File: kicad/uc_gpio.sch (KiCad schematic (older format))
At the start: 1 part, among them U1_501 TMS320F28388DZWTS

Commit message: passed all footprint, preliminarly.. and taken a pic
I've passed all 3d models, and make a pic of that, it's the first
impresion, but it need's more indeed reviews
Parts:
- renumbered U1_501 to U301
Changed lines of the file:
@@
 LCD_GPIO4
 $Comp
-L servo:TMS320F28388 U1_501
+L servo:TMS320F28388 U301
 U 2 1 5DB38FFC
 P 5900 6300
-F 0 "U1_501" H 5900 10873 60  0000 C CNN
+F 0 "U301" H 5900 10873 60  0000 C CNN
 F 1 "TMS320F28388DZWTS" H 5900 10775 50  0000 C CNN
 F 2 "servo:BGA337CP80_19X19_1600X1600X140B50N" H 5900 6300 50  0001 C CNN

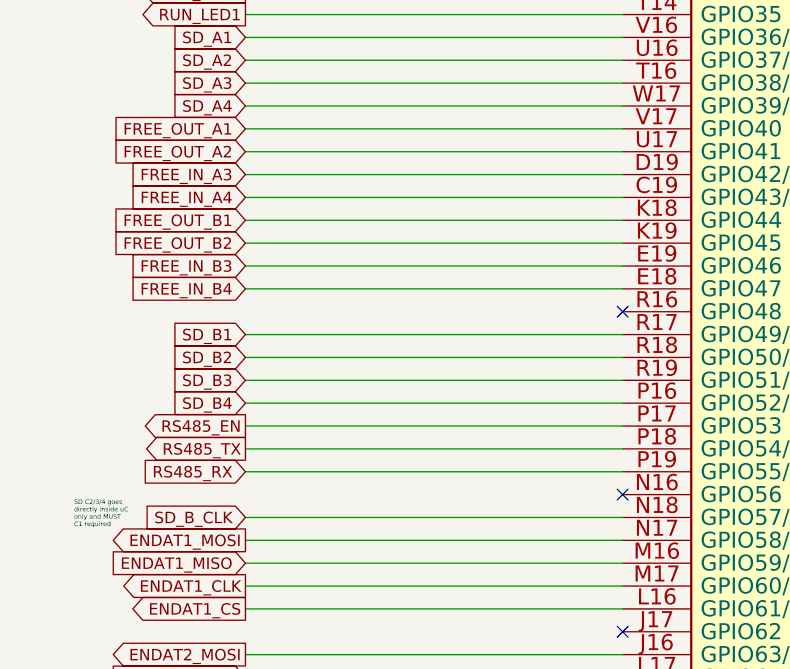
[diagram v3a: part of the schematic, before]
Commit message: I've reducede the PCB size ADC TVS, USB host and IDC out
TVS for ADC protection, USB out 'cause it's almost free and IDC debug
out in an IDC. Better and thinner terminal block connector help in
reduce the board size.
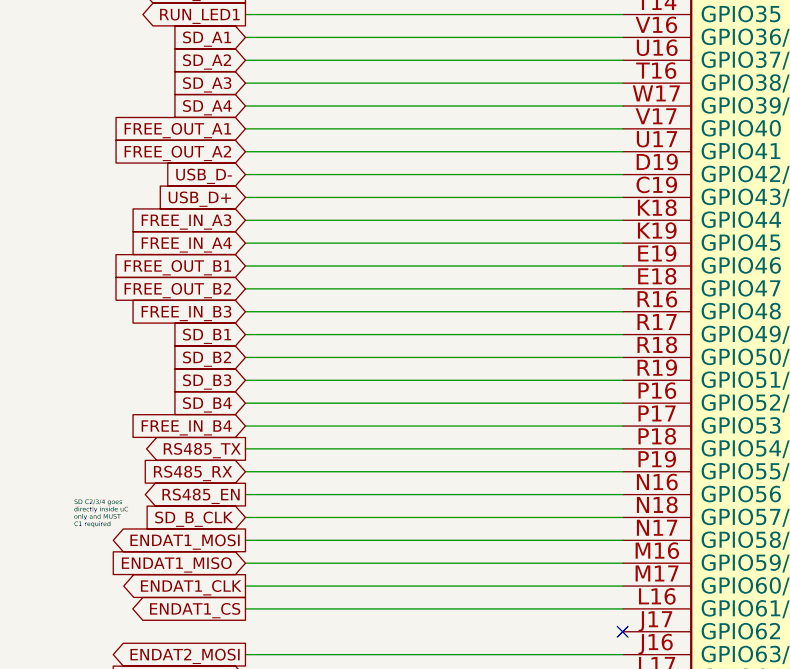
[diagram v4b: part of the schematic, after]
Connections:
- net FREE_IN_A3: now also U301.K18 (GPIO44); no longer U301.D19 (GPIO42/USB0DM)
- net FREE_IN_A4: now also U301.K19 (GPIO45); no longer U301.C19 (GPIO43/USB0DP)
- net FREE_IN_B3: now also U301.R16 (GPIO48); no longer U301.E19 (GPIO46)
- net FREE_IN_B4: now also U301.P17 (GPIO53); no longer U301.E18 (GPIO47)
- net FREE_OUT_B1: now also U301.E19 (GPIO46); no longer U301.K18 (GPIO44)
- net FREE_OUT_B2: now also U301.E18 (GPIO47); no longer U301.K19 (GPIO45)
- net RS485_EN: now also U301.N16 (GPIO56); no longer U301.P17 (GPIO53)
- new net USB_D+: U301.C19 (GPIO43/USB0DP)
- new net USB_D-: U301.D19 (GPIO42/USB0DM)
- no-connect marks 23 -> 21
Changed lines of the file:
@@
 Text GLabel 3150 7500 0    50   Output ~ 0
 RS485_TX
-Text GLabel 3150 7400 0    50   Output ~ 0
+Text GLabel 3150 7700 0    50   Output ~ 0
 RS485_EN
 Wire Wire Line
@@
 Text GLabel 3150 6200 0    50   Input ~ 0
 FREE_OUT_A2
-Text GLabel 3150 6300 0    50   Input ~ 0
+Text GLabel 3150 6500 0    50   Input ~ 0
 FREE_IN_A3
-Text GLabel 3150 6400 0    50   Input ~ 0
+Text GLabel 3150 6600 0    50   Input ~ 0
 FREE_IN_A4
-Text GLabel 3150 6500 0    50   Input ~ 0
+Text GLabel 3150 6700 0    50   Input ~ 0
 FREE_OUT_B1
-Text GLabel 3150 6600 0    50   Input ~ 0
+Text GLabel 3150 6800 0    50   Input ~ 0
 FREE_OUT_B2
-Text GLabel 3150 6700 0    50   Input ~ 0
+Text GLabel 3150 6900 0    50   Input ~ 0
 FREE_IN_B3
-Text GLabel 3150 6800 0    50   Input ~ 0
+Text GLabel 3150 7400 0    50   Input ~ 0
 FREE_IN_B4
 Wire Wire Line
@@
 NoConn ~ 4800 9600
 NoConn ~ 4800 9700
-NoConn ~ 4800 6900
-NoConn ~ 4800 7700
 NoConn ~ 4800 8300
 NoConn ~ 8350 3400
@@
 Text GLabel 9700 3200 2    50   Input ~ 0
 LCD_GPIO4
+Wire Wire Line
+	9700 3200 8350 3200
+Wire Wire Line
+	8350 3300 9700 3300
+Text GLabel 3150 6400 0    50   Input ~ 0
+USB_D+
+Text GLabel 3150 6300 0    50   Input ~ 0
+USB_D-
 $Comp
 L servo:TMS320F28388 U301
@@
 $EndComp
 Wire Wire Line
-	9700 3200 8350 3200
-Wire Wire Line
-	8350 3300 9700 3300
+	4800 6900 3150 6900
+Wire Wire Line
+	4800 7700 3150 7700
 $EndSCHEMATC

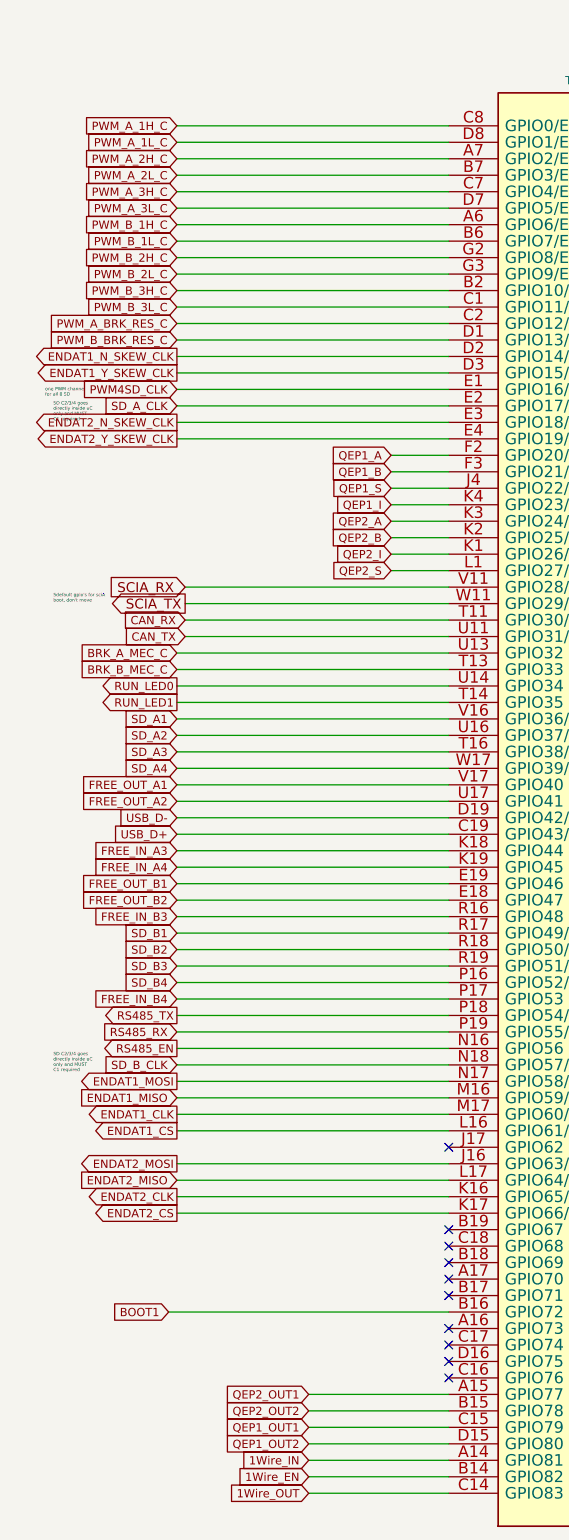
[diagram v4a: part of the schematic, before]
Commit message: I forgot that QUEP was diferential!! all to back....
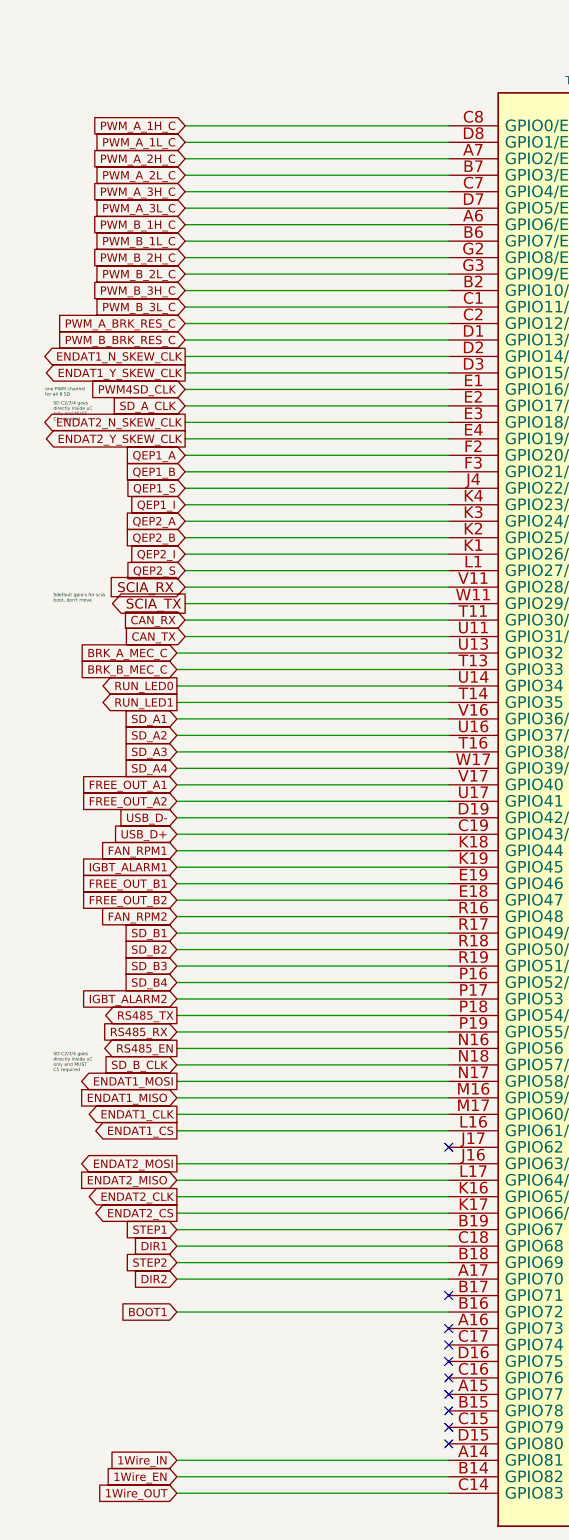
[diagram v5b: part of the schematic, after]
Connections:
- net DIR2: now reaches U301.A17 (GPIO70)
- net STEP2: now reaches U301.B18 (GPIO69)
- net STEP1: now reaches U301.B19 (GPIO67)
- net DIR1: now reaches U301.C18 (GPIO68)
- net FREE_IN_A3 renamed FAN_RPM1
- net FREE_IN_A4 renamed IGBT_ALARM1
- net FREE_IN_B3 renamed FAN_RPM2
- net FREE_IN_B4 renamed IGBT_ALARM2
- net QEP1_OUT1: no longer names the net of U301.C15 (GPIO79)
- net QEP1_OUT2: no longer names the net of U301.D15 (GPIO80)
- net QEP2_OUT1: no longer names the net of U301.A15 (GPIO77)
- net QEP2_OUT2: no longer names the net of U301.B15 (GPIO78)
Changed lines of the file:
@@
 $Descr A3 16535 11693
 encoding utf-8
-Sheet 13 18
+Sheet 13 19
 Title "gpio"
 Date "2020-01-09"
@@
 $EndDescr
 Wire Wire Line
-	3950 10400 4800 10400
-Wire Wire Line
-	3950 10300 4800 10300
-Wire Wire Line
-	3950 10200 4800 10200
-Wire Wire Line
-	3950 10100 4800 10100
-Wire Wire Line
-	3950 10000 4800 10000
-Wire Wire Line
-	3950 9900 4800 9900
-Wire Wire Line
-	3950 9800 4800 9800
-Text GLabel 3150 2100 0    50   Input ~ 0
+	3150 10400 4800 10400
+Wire Wire Line
+	3150 10300 4800 10300
+Wire Wire Line
+	3150 10200 4800 10200
+Text GLabel 3200 2100 0    50   Input ~ 0
 PWM_A_1H_C
-Text GLabel 3150 2300 0    50   Input ~ 0
+Text GLabel 3200 2300 0    50   Input ~ 0
 PWM_A_2H_C
-Text GLabel 3150 2500 0    50   Input ~ 0
+Text GLabel 3200 2500 0    50   Input ~ 0
 PWM_A_3H_C
-Text GLabel 3150 2200 0    50   Input ~ 0
+Text GLabel 3200 2200 0    50   Input ~ 0
 PWM_A_1L_C
-Text GLabel 3150 2400 0    50   Input ~ 0
+Text GLabel 3200 2400 0    50   Input ~ 0
 PWM_A_2L_C
-Text GLabel 3150 2600 0    50   Input ~ 0
+Text GLabel 3200 2600 0    50   Input ~ 0
 PWM_A_3L_C
-Text GLabel 3150 2900 0    50   Input ~ 0
+Text GLabel 3200 2900 0    50   Input ~ 0
 PWM_B_2H_C
-Text GLabel 3150 2700 0    50   Input ~ 0
+Text GLabel 3200 2700 0    50   Input ~ 0
 PWM_B_1H_C
-Text GLabel 3150 2800 0    50   Input ~ 0
+Text GLabel 3200 2800 0    50   Input ~ 0
 PWM_B_1L_C
-Text GLabel 3150 3100 0    50   Input ~ 0
+Text GLabel 3200 3100 0    50   Input ~ 0
 PWM_B_3H_C
-Text GLabel 3150 3200 0    50   Input ~ 0
+Text GLabel 3200 3200 0    50   Input ~ 0
 PWM_B_3L_C
-Text GLabel 3150 3000 0    50   Input ~ 0
+Text GLabel 3200 3000 0    50   Input ~ 0
 PWM_B_2L_C
 Wire Wire Line
@@
 Wire Wire Line
 	3150 5600 4800 5600
-Text GLabel 3100 9300 0    50   Input ~ 0
+Text GLabel 3150 9300 0    50   Input ~ 0
 BOOT1
 Text GLabel 9750 2100 2    50   Input ~ 0
@@
 	8350 2100 9750 2100
 Wire Wire Line
-	3100 9300 4800 9300
+	3150 9300 4800 9300
 Text GLabel 3200 5000 0    60   Output ~ 0
 SCIA_TX
@@
 Wire Wire Line
 	3150 8700 4800 8700
-Text GLabel 4450 4500 0    50   Input ~ 0
+Text GLabel 3200 4500 0    50   Input ~ 0
 QEP2_A
-Text GLabel 4450 4600 0    50   Input ~ 0
+Text GLabel 3200 4600 0    50   Input ~ 0
 QEP2_B
-Text GLabel 4450 4700 0    50   Input ~ 0
+Text GLabel 3200 4700 0    50   Input ~ 0
 QEP2_I
-Text GLabel 4450 4100 0    50   Input ~ 0
+Text GLabel 3200 4100 0    50   Input ~ 0
 QEP1_A
-Text GLabel 4450 4200 0    50   Input ~ 0
+Text GLabel 3200 4200 0    50   Input ~ 0
 QEP1_B
-Text GLabel 4450 4400 0    50   Input ~ 0
+Text GLabel 3200 4400 0    50   Input ~ 0
 QEP1_I
 Wire Wire Line
@@
 CAN_RX
 Wire Wire Line
-	3150 3900 4800 3900
-Wire Wire Line
-	3150 4000 4800 4000
+	3200 3900 4800 3900
+Wire Wire Line
+	3200 4000 4800 4000
 Wire Wire Line
 	3150 5700 4800 5700
@@
 	3150 6000 4800 6000
 Wire Wire Line
-	3150 2200 4800 2200
-Wire Wire Line
-	3150 2300 4800 2300
-Wire Wire Line
-	3150 2400 4800 2400
-Wire Wire Line
-	3150 2500 4800 2500
-Wire Wire Line
-	3150 2600 4800 2600
-Wire Wire Line
-	3150 2700 4800 2700
-Wire Wire Line
-	3150 2800 4800 2800
-Wire Wire Line
-	3150 2900 4800 2900
-Wire Wire Line
-	3150 3000 4800 3000
-Wire Wire Line
-	3150 3100 4800 3100
-Wire Wire Line
-	3150 3200 4800 3200
-Wire Wire Line
-	3150 3400 4800 3400
-Wire Wire Line
-	3150 3300 4800 3300
+	3200 2200 4800 2200
+Wire Wire Line
+	3200 2300 4800 2300
+Wire Wire Line
+	3200 2400 4800 2400
+Wire Wire Line
+	3200 2500 4800 2500
+Wire Wire Line
+	3200 2600 4800 2600
+Wire Wire Line
+	3200 2700 4800 2700
+Wire Wire Line
+	3200 2800 4800 2800
+Wire Wire Line
+	3200 2900 4800 2900
+Wire Wire Line
+	3200 3000 4800 3000
+Wire Wire Line
+	3200 3100 4800 3100
+Wire Wire Line
+	3200 3200 4800 3200
+Wire Wire Line
+	3200 3400 4800 3400
+Wire Wire Line
+	3200 3300 4800 3300
 Wire Wire Line
 	3200 4900 4800 4900
@@
 Text GLabel 3150 6000 0    50   Input ~ 0
 SD_A4
-Text GLabel 3150 3300 0    50   Input ~ 0
+Text GLabel 3200 3300 0    50   Input ~ 0
 PWM_A_BRK_RES_C
-Text GLabel 3150 3400 0    50   Input ~ 0
+Text GLabel 3200 3400 0    50   Input ~ 0
 PWM_B_BRK_RES_C
 Text GLabel 3150 7000 0    50   Input ~ 0
@@
 SD C2/3/4 goes \ndirectly inside uC\nonly and MUST  \nC1 required
 Wire Wire Line
-	3150 3800 4800 3800
-Text GLabel 3150 3800 0    50   Input ~ 0
+	3200 3800 4800 3800
+Text GLabel 3200 3800 0    50   Input ~ 0
 SD_A_CLK
-Text GLabel 3150 3700 0    50   Input ~ 0
+Text GLabel 3200 3700 0    50   Input ~ 0
 PWM4SD_CLK
 Wire Wire Line
-	3150 3700 4800 3700
+	3200 3700 4800 3700
 Text Notes 2350 3750 0    20   ~ 0
 one PWM channel \nfor all 8 SD
@@
 Sdefault gpio's for sciA \nboot, don't move
 Wire Wire Line
-	4450 4100 4800 4100
-Wire Wire Line
-	4450 4200 4800 4200
-Wire Wire Line
-	4450 4300 4800 4300
-Text GLabel 4450 4300 0    50   Input ~ 0
+	3200 4100 4800 4100
+Wire Wire Line
+	3200 4200 4800 4200
+Wire Wire Line
+	3200 4300 4800 4300
+Text GLabel 3200 4300 0    50   Input ~ 0
 QEP1_S
 Wire Wire Line
-	4450 4400 4800 4400
-Text GLabel 4450 4800 0    50   Input ~ 0
+	3200 4400 4800 4400
+Text GLabel 3200 4800 0    50   Input ~ 0
 QEP2_S
 Wire Wire Line
-	4450 4700 4800 4700
-Wire Wire Line
-	4450 4600 4800 4600
-Wire Wire Line
-	4450 4500 4800 4500
-Wire Wire Line
-	4450 4800 4800 4800
+	3200 4700 4800 4700
+Wire Wire Line
+	3200 4600 4800 4600
+Wire Wire Line
+	3200 4500 4800 4500
+Wire Wire Line
+	3200 4800 4800 4800
 Wire Wire Line
 	3150 6100 4800 6100
@@
 Text GLabel 9700 7500 2    50   Input ~ 0
 ECAT1_RX_ER
-Text GLabel 3150 3500 0    50   Output ~ 0
+Text GLabel 3200 3500 0    50   Output ~ 0
 ENDAT1_N_SKEW_CLK
-Text GLabel 3150 3600 0    50   Output ~ 0
+Text GLabel 3200 3600 0    50   Output ~ 0
 ENDAT1_Y_SKEW_CLK
 Wire Wire Line
-	3150 3500 4800 3500
-Wire Wire Line
-	3150 3600 4800 3600
-Text GLabel 3150 3900 0    50   Output ~ 0
+	3200 3500 4800 3500
+Wire Wire Line
+	3200 3600 4800 3600
+Text GLabel 3200 3900 0    50   Output ~ 0
 ENDAT2_N_SKEW_CLK
-Text GLabel 3150 4000 0    50   Output ~ 0
+Text GLabel 3200 4000 0    50   Output ~ 0
 ENDAT2_Y_SKEW_CLK
 Wire Wire Line
@@
 Text GLabel 3150 6200 0    50   Input ~ 0
 FREE_OUT_A2
-Text GLabel 3150 6500 0    50   Input ~ 0
-FREE_IN_A3
-Text GLabel 3150 6600 0    50   Input ~ 0
-FREE_IN_A4
 Text GLabel 3150 6700 0    50   Input ~ 0
 FREE_OUT_B1
 Text GLabel 3150 6800 0    50   Input ~ 0
 FREE_OUT_B2
-Text GLabel 3150 6900 0    50   Input ~ 0
-FREE_IN_B3
-Text GLabel 3150 7400 0    50   Input ~ 0
-FREE_IN_B4
-Wire Wire Line
-	3150 2100 4800 2100
+Wire Wire Line
+	3200 2100 4800 2100
 Text GLabel 3150 5400 0    50   Input ~ 0
 BRK_B_MEC_C
@@
 Wire Wire Line
 	8350 9600 9700 9600
-Text GLabel 3950 10400 0    50   Input ~ 0
+Text GLabel 3150 10400 0    50   Input ~ 0
 1Wire_OUT
-Text GLabel 3950 10200 0    50   Input ~ 0
+Text GLabel 3150 10200 0    50   Input ~ 0
 1Wire_IN
-Text GLabel 3950 10300 0    50   Input ~ 0
+Text GLabel 3150 10300 0    50   Input ~ 0
 1Wire_EN
-Text GLabel 3950 9800 0    50   Input ~ 0
-QEP2_OUT1
-Text GLabel 3950 9900 0    50   Input ~ 0
-QEP2_OUT2
-Text GLabel 3950 10000 0    50   Input ~ 0
-QEP1_OUT1
-Text GLabel 3950 10100 0    50   Input ~ 0
-QEP1_OUT2
-NoConn ~ 4800 8800
-NoConn ~ 4800 8900
-NoConn ~ 4800 9000
-NoConn ~ 4800 9100
 NoConn ~ 4800 9200
 NoConn ~ 4800 9400
@@
 Text GLabel 3150 6300 0    50   Input ~ 0
 USB_D-
+Wire Wire Line
+	4800 6900 3150 6900
+Wire Wire Line
+	4800 7700 3150 7700
+Text GLabel 3150 6900 0    50   Input ~ 0
+FAN_RPM2
+Text GLabel 3150 7400 0    50   Input ~ 0
+IGBT_ALARM2
+Text GLabel 3150 6500 0    50   Input ~ 0
+FAN_RPM1
+Text GLabel 3150 6600 0    50   Input ~ 0
+IGBT_ALARM1
+Text GLabel 3150 8800 0    50   Input ~ 0
+STEP1
+Text GLabel 3150 8900 0    50   Input ~ 0
+DIR1
 $Comp
 L servo:TMS320F28388 U301
@@
 $EndComp
 Wire Wire Line
-	4800 6900 3150 6900
-Wire Wire Line
-	4800 7700 3150 7700
+	3150 9000 4800 9000
+Wire Wire Line
+	3150 9100 4800 9100
+Wire Wire Line
+	3150 8900 4800 8900
+Wire Wire Line
+	3150 8800 4800 8800
+Text GLabel 3150 9000 0    50   Input ~ 0
+STEP2
+Text GLabel 3150 9100 0    50   Input ~ 0
+DIR2
+NoConn ~ 4800 9800
+NoConn ~ 4800 9900
+NoConn ~ 4800 10000
+NoConn ~ 4800 10100
 $EndSCHEMATC

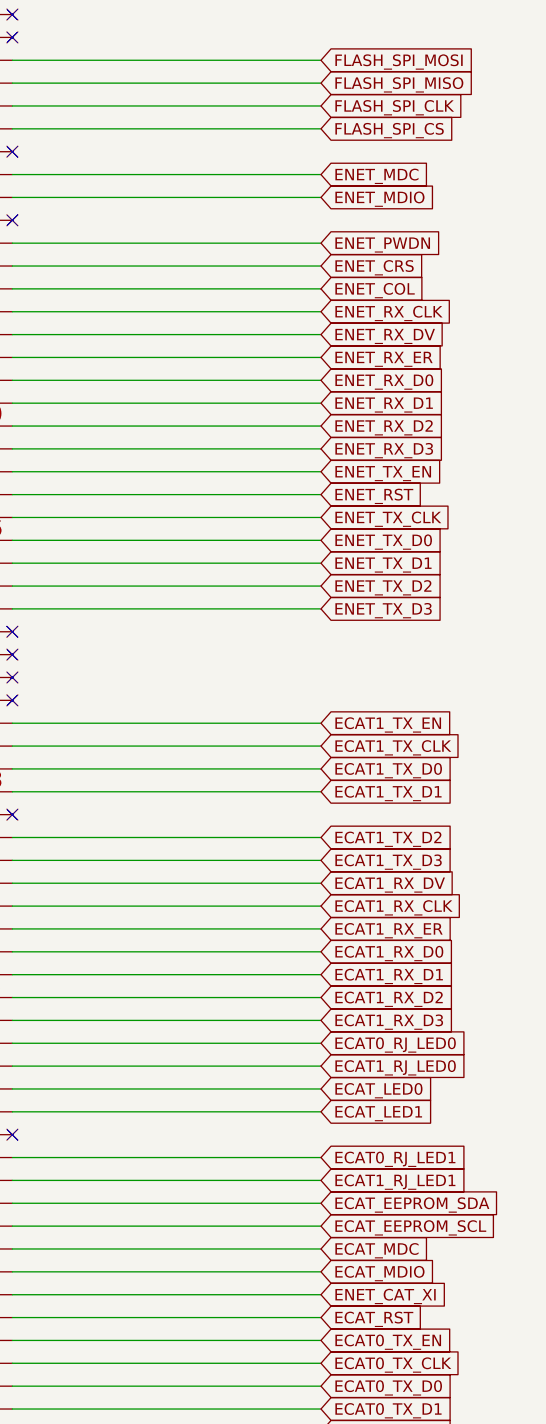
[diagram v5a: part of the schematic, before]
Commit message: All IC placed inside board size but....
I've placed all stuff on board size even thought all are in groups I've
to move the IC to route them. Let's begin
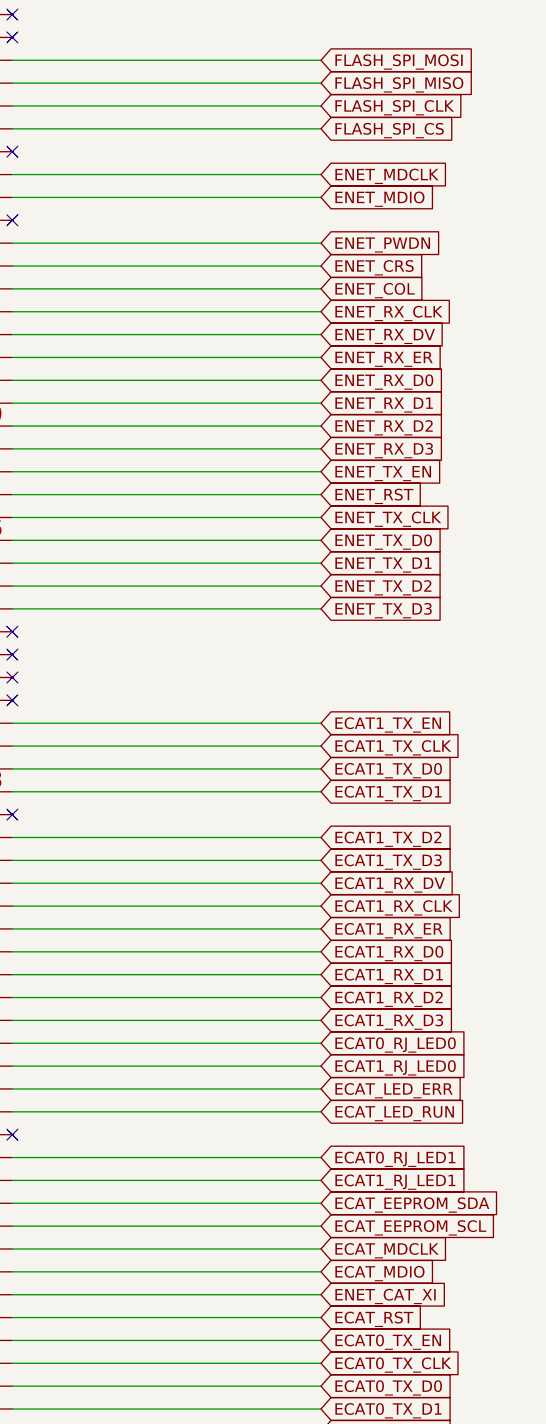
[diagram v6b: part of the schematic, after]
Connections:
- net ECAT_LED0 renamed ECAT_LED_ERR
- net ECAT_LED1 renamed ECAT_LED_RUN
- net ECAT_MDC renamed ECAT_MDCLK
- net ENET_MDC renamed ENET_MDCLK
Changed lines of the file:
@@
 Text GLabel 9700 9000 2    50   Input ~ 0
 ECAT_MDIO
-Text GLabel 9700 8900 2    50   Input ~ 0
-ECAT_MDC
 Text GLabel 9700 9200 2    50   Input ~ 0
 ECAT_RST
@@
 ENET_MDIO
 Text GLabel 9700 4200 2    50   Input ~ 0
-ENET_MDC
+ENET_MDCLK
 Text GLabel 9700 5600 2    50   Input ~ 0
 ENET_RST
@@
 ECAT0_RJ_LED0
 Text GLabel 9700 8300 2    50   Input ~ 0
-ECAT_LED1
+ECAT_LED_RUN
 Text GLabel 9700 8200 2    50   Input ~ 0
-ECAT_LED0
+ECAT_LED_ERR
 Text GLabel 9700 8100 2    50   Input ~ 0
 ECAT1_RJ_LED0
@@
 NoConn ~ 4800 10000
 NoConn ~ 4800 10100
+Text GLabel 9700 8900 2    50   Input ~ 0
+ECAT_MDCLK
 $EndSCHEMATC
